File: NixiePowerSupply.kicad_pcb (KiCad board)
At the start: 2 copper layers, 41.5 x 41.5 mm, 20 parts, among them J1 Conn_01x02, J2 Conn_01x02, Q1 IRF740, Q2 2N3905, U1 MC34063AP

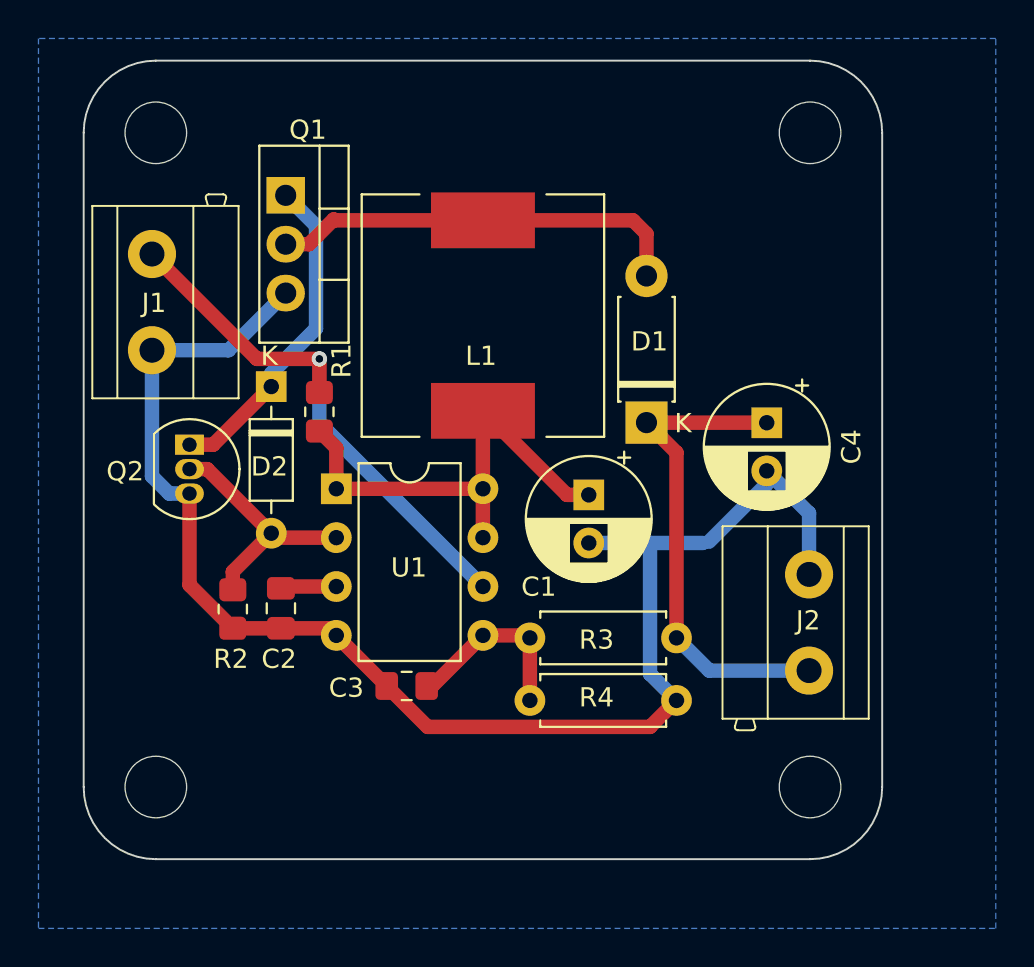
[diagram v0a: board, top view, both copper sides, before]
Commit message: mark input, output
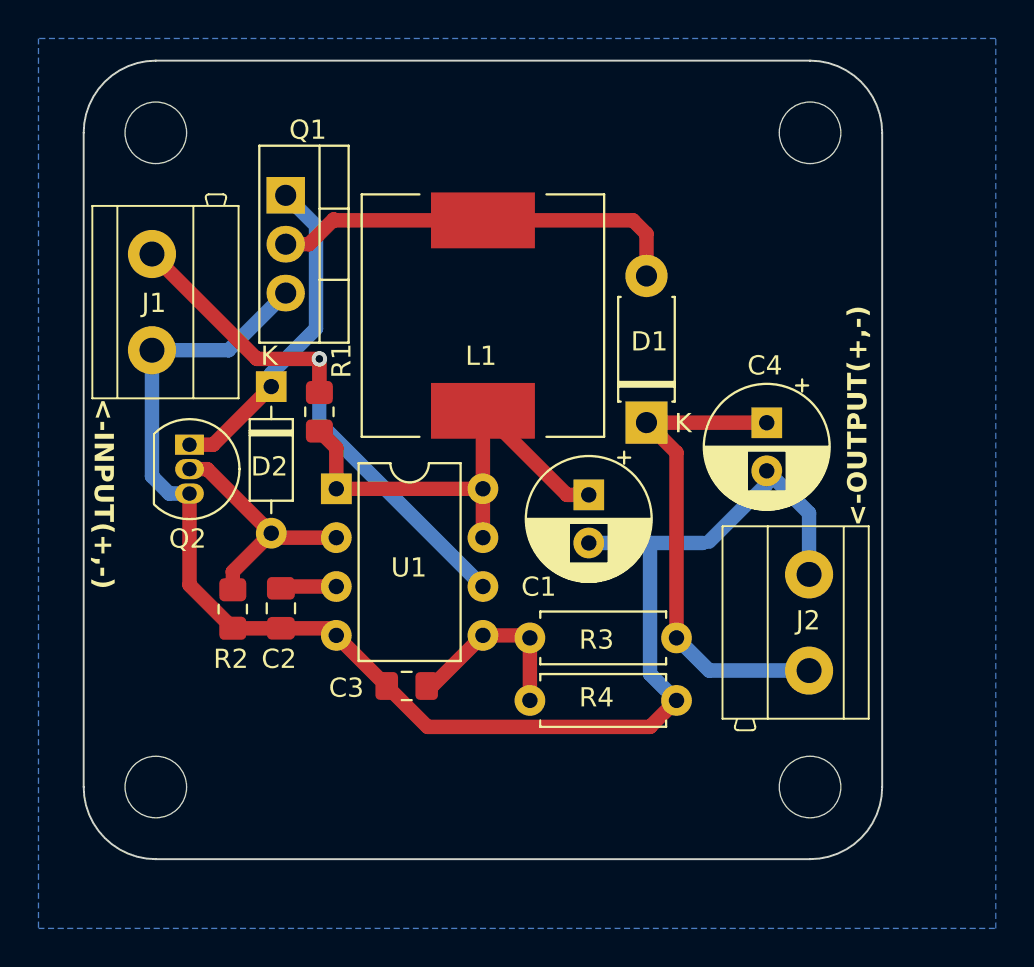
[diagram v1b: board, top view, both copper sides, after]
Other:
- board text added: "<-INPUT(+,-)"
- board text added: "<-OUTPUT(+,-)"
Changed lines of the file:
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@@
     (fp_line (start 1 0.625) (end -1 0.625)
       (stroke (width 0.1) (type solid)) (layer "F.Fab"))
-    (pad "1" smd roundrect (at -1.0375 0 270) (size 1.175 1.45) (layers "F.Cu" "F.Paste" "F.Mask") (roundrect_rratio 0.212766)
+    (pad "1" smd roundrect (at -1.0375 0 270) (size 1.175 1.45) (layers "F.Cu" "F.Paste" "F.Mask") (roundrect_rratio 0.2127659574)
       (net 3 "Net-(U1-TC)") (pintype "passive"))
-    (pad "2" smd roundrect (at 1.0375 0 270) (size 1.175 1.45) (layers "F.Cu" "F.Paste" "F.Mask") (roundrect_rratio 0.212766)
+    (pad "2" smd roundrect (at 1.0375 0 270) (size 1.175 1.45) (layers "F.Cu" "F.Paste" "F.Mask") (roundrect_rratio 0.2127659574)
       (net 2 "GND") (pintype "passive"))
     (model "${KICAD6_3DMODEL_DIR}/Capacitor_SMD.3dshapes/C_0805_2012Metric.wrl"
@@
     (property "ki_keywords" "cap capacitor")
     (attr through_hole)
-    (fp_text reference "C4" (at 1.25 -4.4 90) (layer "F.SilkS")
+    (fp_text reference "C4" (at -2.969271 0.09835 -180) (layer "F.SilkS")
         (effects (font (size 1 1) (thickness 0.15)))
     )
@@
     (fp_line (start 1 0.625) (end -1 0.625)
       (stroke (width 0.1) (type solid)) (layer "F.Fab"))
-    (pad "1" smd roundrect (at -1 0 270) (size 1.2 1.4) (layers "F.Cu" "F.Paste" "F.Mask") (roundrect_rratio 0.208333)
+    (pad "1" smd roundrect (at -1 0 270) (size 1.2 1.4) (layers "F.Cu" "F.Paste" "F.Mask") (roundrect_rratio 0.2083333333)
       (net 9 "Net-(J1-Pin_1)") (pintype "passive"))
-    (pad "2" smd roundrect (at 1 0 270) (size 1.2 1.4) (layers "F.Cu" "F.Paste" "F.Mask") (roundrect_rratio 0.208333)
+    (pad "2" smd roundrect (at 1 0 270) (size 1.2 1.4) (layers "F.Cu" "F.Paste" "F.Mask") (roundrect_rratio 0.2083333333)
       (net 1 "Net-(U1-DC)") (pintype "passive"))
     (model "${KICAD6_3DMODEL_DIR}/Resistor_SMD.3dshapes/R_0805_2012Metric.wrl"
@@
     (fp_line (start 1 0.625) (end -1 0.625)
       (stroke (width 0.1) (type solid)) (layer "F.Fab"))
-    (pad "1" smd roundrect (at -1 0 270) (size 1.2 1.4) (layers "F.Cu" "F.Paste" "F.Mask") (roundrect_rratio 0.208333)
+    (pad "1" smd roundrect (at -1 0 270) (size 1.2 1.4) (layers "F.Cu" "F.Paste" "F.Mask") (roundrect_rratio 0.2083333333)
       (net 8 "Net-(D2-A)") (pintype "passive"))
-    (pad "2" smd roundrect (at 1 0 270) (size 1.2 1.4) (layers "F.Cu" "F.Paste" "F.Mask") (roundrect_rratio 0.208333)
+    (pad "2" smd roundrect (at 1 0 270) (size 1.2 1.4) (layers "F.Cu" "F.Paste" "F.Mask") (roundrect_rratio 0.2083333333)
       (net 2 "GND") (pintype "passive"))
     (model "${KICAD6_3DMODEL_DIR}/Resistor_SMD.3dshapes/R_0805_2012Metric.wrl"
@@
     (property "ki_keywords" "PNP Transistor")
     (attr through_hole)
-    (fp_text reference "Q2" (at 1.38835 3.34835 -180) (layer "F.SilkS")
+    (fp_text reference "Q2" (at 4.88835 0.09835 -180) (layer "F.SilkS")
         (effects (font (size 1 1) (thickness 0.15)))
     )
@@
     (fp_line (start 1 0.625) (end -1 0.625)
       (stroke (width 0.1) (type solid)) (layer "F.Fab"))
-    (pad "1" smd roundrect (at -1.0375 0 180) (size 1.175 1.45) (layers "F.Cu" "F.Paste" "F.Mask") (roundrect_rratio 0.212766)
+    (pad "1" smd roundrect (at -1.0375 0 180) (size 1.175 1.45) (layers "F.Cu" "F.Paste" "F.Mask") (roundrect_rratio 0.2127659574)
       (net 4 "Net-(U1-Vfb)") (pintype "passive"))
-    (pad "2" smd roundrect (at 1.0375 0 180) (size 1.175 1.45) (layers "F.Cu" "F.Paste" "F.Mask") (roundrect_rratio 0.212766)
+    (pad "2" smd roundrect (at 1.0375 0 180) (size 1.175 1.45) (layers "F.Cu" "F.Paste" "F.Mask") (roundrect_rratio 0.2127659574)
       (net 2 "GND") (pintype "passive"))
     (model "${KICAD6_3DMODEL_DIR}/Capacitor_SMD.3dshapes/C_0805_2012Metric.wrl"
@@
   (gr_arc (start 131.09835 150.40165) (mid 130 153.0533) (end 127.34835 154.15165)
     (stroke (width 0.1) (type default)) (layer "Edge.Cuts"))
+  (gr_text "<-INPUT(+,-)" (at 90.04835 130.20165 270) (layer "F.SilkS")
+    (effects (font (size 1 1) (thickness 0.2) bold) (justify left bottom))
+  )
+  (gr_text "<-OUTPUT(+,-)" (at 130.39835 136.85165 90) (layer "F.SilkS")
+    (effects (font (size 1 1) (thickness 0.2) bold) (justify left bottom))
+  )
   (segment (start 114.71597 135.21927) (end 110.34835 130.85165) (width 0.75) (layer "F.Cu") (net 1))
   (segment (start 102.72835 132.78165) (end 101.84835 131.90165) (width 0.75) (layer "F.Cu") (net 1))

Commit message: add logos
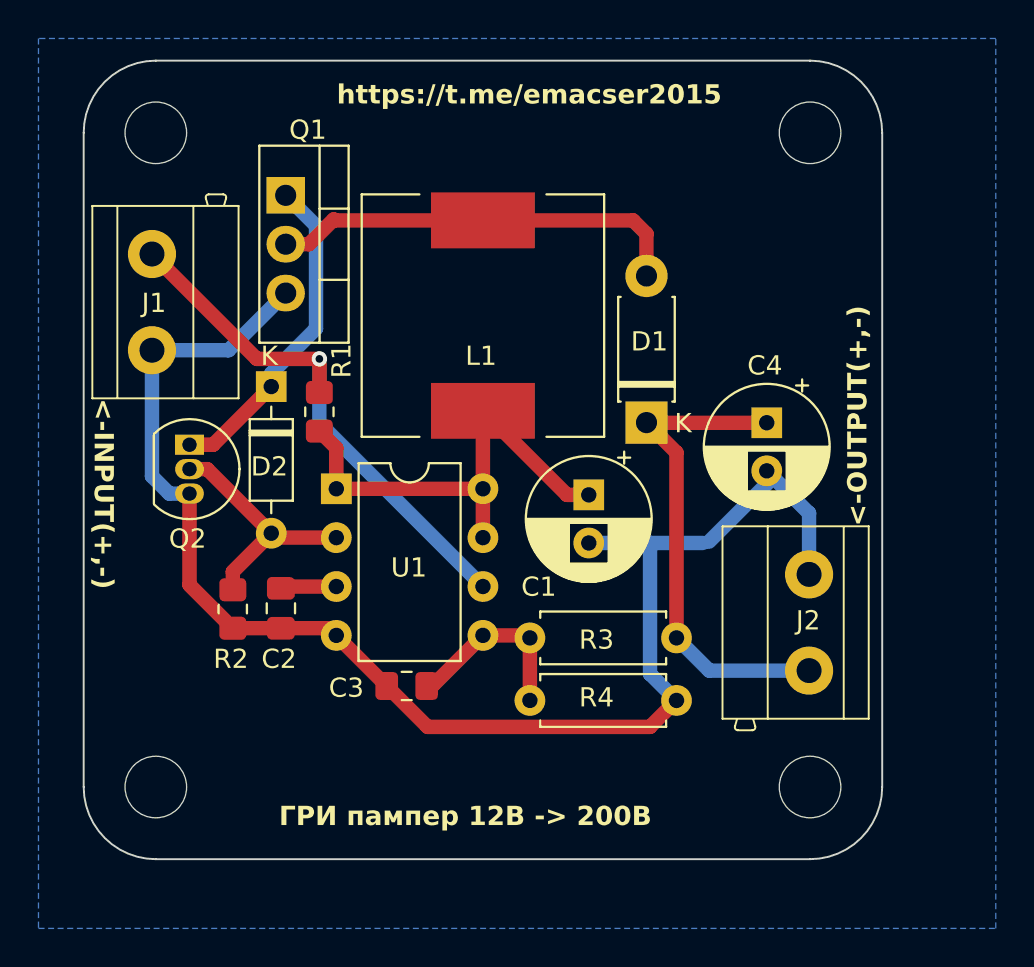
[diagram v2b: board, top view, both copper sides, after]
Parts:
- added G***: LOGO, Library:logo, B.Cu at (102.0, 150.8)
- added REF**: KiCad-Logo2_6mm_SilkScreen, Symbol:KiCad-Logo2_6mm_SilkScreen, B.Cu at (111.2, 116.0)
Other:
- board text added: "https://t.me/emacser2015"
- board text added: "ГРИ пампер 12В -> 200В"

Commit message: add ibom
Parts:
- C1: value C_Polarized -> 220uF 16V LESR Polar 6.3x2.5
- C2: value C -> 2200pF, 0805
- C3: value C -> 0.01uF, 0805
- C4: value C_Polarized -> 2.2uF 250V Polar 6.3x2.5
- D1: value D -> UF4004 UF4007, DO-41
- D2: value D -> 1N4148 1N914, DO-35
- J1, J2: value Conn_01x02 -> DG301-5.0-2P
- L1: value L -> 220uH, 12x12
- Q1: value IRF740 -> IRF740, TO-220
- Q2: value 2N3905 -> MPSA55, TO-92
- R1: value R -> 0.33, 0805
- R2: value R -> 1K, 0805
- R3: value R -> 475K, 1%
- R4: value R -> 3K32, 1%
- U1: value MC34063AP -> MC34063
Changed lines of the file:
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@@
         (effects (font (size 1 1) (thickness 0.15)))
     )
-    (fp_text value "Conn_01x02" (at 0.05 -5.8 90) (layer "F.Fab")
+    (fp_text value "DG301-5.0-2P" (at 0.05 -5.8 90) (layer "F.Fab")
         (effects (font (size 1 1) (thickness 0.15)))
     )
@@
         (effects (font (size 1 1) (thickness 0.15)))
     )
-    (fp_text value "C" (at 0 1.68 90) (layer "F.Fab")
+    (fp_text value "2200pF, 0805" (at 0 1.68 90) (layer "F.Fab")
         (effects (font (size 1 1) (thickness 0.15)))
     )
@@
     (descr "CP, Radial series, Radial, pin pitch=2.50mm, , diameter=6.3mm, Electrolytic Capacitor")
     (tags "CP Radial series Radial pin pitch 2.50mm  diameter 6.3mm Electrolytic Capacitor")
+    (property "Link" "https://www.chipdip.ru/product0/9000565820")
     (property "Sheetfile" "NixiePowerSupply.kicad_sch")
     (property "Sheetname" "")
@@
         (effects (font (size 1 1) (thickness 0.15)))
     )
-    (fp_text value "C_Polarized" (at 1.25 4.4 90) (layer "F.Fab")
+    (fp_text value "2.2uF 250V Polar 6.3x2.5" (at 1.25 4.4 90) (layer "F.Fab")
         (effects (font (size 1 1) (thickness 0.15)))
     )
@@
         (effects (font (size 1 1) (thickness 0.15)))
     )
-    (fp_text value "R" (at 3.81 2.37) (layer "F.Fab")
+    (fp_text value "3K32, 1%" (at 3.81 2.37) (layer "F.Fab")
         (effects (font (size 1 1) (thickness 0.15)))
     )
@@
         (effects (font (size 1 1) (thickness 0.15)))
     )
-    (fp_text value "D" (at 3.81 2.47 90) (layer "F.Fab")
+    (fp_text value "UF4004 UF4007, DO-41" (at 3.81 2.47 90) (layer "F.Fab")
         (effects (font (size 1 1) (thickness 0.15)))
     )
@@
         (effects (font (size 1 1) (thickness 0.15)))
     )
-    (fp_text value "D" (at 3.81 2.12 90) (layer "F.Fab")
+    (fp_text value "1N4148 1N914, DO-35" (at 3.81 2.12 90) (layer "F.Fab")
         (effects (font (size 1 1) (thickness 0.15)))
     )
@@
         (effects (font (size 1 1) (thickness 0.15)))
     )
-    (fp_text value "R" (at 0 1.65 90) (layer "F.Fab")
+    (fp_text value "0.33, 0805" (at 0 1.65 90) (layer "F.Fab")
         (effects (font (size 1 1) (thickness 0.15)))
     )
@@
         (effects (font (size 1 1) (thickness 0.15)))
     )
-    (fp_text value "R" (at 0 1.65 90) (layer "F.Fab")
+    (fp_text value "1K, 0805" (at 0 1.65 90) (layer "F.Fab")
         (effects (font (size 1 1) (thickness 0.15)))
     )
@@
         (effects (font (size 1 1) (thickness 0.15)))
     )
-    (fp_text value "L" (at 0 7.6 90) (layer "F.Fab")
+    (fp_text value "220uH, 12x12" (at 0 7.6 90) (layer "F.Fab")
         (effects (font (size 1 1) (thickness 0.15)))
     )
@@
         (effects (font (size 1 1) (thickness 0.15)))
     )
-    (fp_text value "IRF740" (at 2.54 2.5 90) (layer "F.Fab")
+    (fp_text value "IRF740, TO-220" (at 2.54 2.5 90) (layer "F.Fab")
         (effects (font (size 1 1) (thickness 0.15)))
     )
@@
     (descr "CP, Radial series, Radial, pin pitch=2.50mm, , diameter=6.3mm, Electrolytic Capacitor")
     (tags "CP Radial series Radial pin pitch 2.50mm  diameter 6.3mm Electrolytic Capacitor")
+    (property "Link" "https://www.chipdip.ru/product0/9000565757")
     (property "Sheetfile" "NixiePowerSupply.kicad_sch")
     (property "Sheetname" "")
@@
         (effects (font (size 1 1) (thickness 0.15)))
     )
-    (fp_text value "C_Polarized" (at 1.25 4.4 90) (layer "F.Fab")
+    (fp_text value "220uF 16V LESR Polar 6.3x2.5" (at 1.25 4.4 90) (layer "F.Fab")
         (effects (font (size 1 1) (thickness 0.15)))
     )
@@
         (effects (font (size 1 1) (thickness 0.15)))
     )
-    (fp_text value "MC34063AP" (at 3.81 9.95) (layer "F.Fab")
+    (fp_text value "MC34063" (at 3.81 9.95) (layer "F.Fab")
         (effects (font (size 1 1) (thickness 0.15)))
     )
@@
         (effects (font (size 1 1) (thickness 0.15)))
     )
-    (fp_text value "Conn_01x02" (at 0.05 -5.8 90) (layer "F.Fab")
+    (fp_text value "DG301-5.0-2P" (at 0.05 -5.8 90) (layer "F.Fab")
         (effects (font (size 1 1) (thickness 0.15)))
     )
@@
         (effects (font (size 1 1) (thickness 0.15)))
     )
-    (fp_text value "R" (at 3.81 2.37) (layer "F.Fab")
+    (fp_text value "475K, 1%" (at 3.81 2.37) (layer "F.Fab")
         (effects (font (size 1 1) (thickness 0.15)))
     )
@@
         (effects (font (size 1 1) (thickness 0.15)))
     )
-    (fp_text value "2N3905" (at 1.27 2.79 90) (layer "F.Fab")
+    (fp_text value "MPSA55, TO-92" (at 1.27 2.79 90) (layer "F.Fab")
         (effects (font (size 1 1) (thickness 0.15)))
     )
@@
         (effects (font (size 1 1) (thickness 0.15)))
     )
-    (fp_text value "C" (at 0 1.68) (layer "F.Fab")
-        (effects (font (size 1 1) (thickness 0.15)))
-    )
+    (fp_text value "0.01uF, 0805" (at 0 1.68) (layer "F.Fab")
+        (effects (font (size 1 1) (thickness 0.15)))
+    )

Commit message: fix R3, R4
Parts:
- R3: value 475K, 1% -> 470K, 1%
- R4: value 3K32, 1% -> 3K, 1%
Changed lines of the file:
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@@
         (effects (font (size 1 1) (thickness 0.15)))
     )
-    (fp_text value "3K32, 1%" (at 3.81 2.37) (layer "F.Fab")
+    (fp_text value "3K, 1%" (at 3.81 2.37) (layer "F.Fab")
         (effects (font (size 1 1) (thickness 0.15)))
     )
@@
         (effects (font (size 1 1) (thickness 0.15)))
     )
-    (fp_text value "475K, 1%" (at 3.81 2.37) (layer "F.Fab")
-        (effects (font (size 1 1) (thickness 0.15)))
-    )
+    (fp_text value "470K, 1%" (at 3.81 2.37) (layer "F.Fab")
+        (effects (font (size 1 1) (thickness 0.15)))
+    )

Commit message: fix links in bom
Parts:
- Q2: value MPSA55, TO-92 -> MPSA56, TO-92
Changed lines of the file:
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@@
     (descr "Capacitor SMD 0805 (2012 Metric), square (rectangular) end terminal, IPC_7351 nominal with elongated pad for handsoldering. (Body size source: IPC-SM-782 page 76, https://www.pcb-3d.com/wordpress/wp-content/uploads/ipc-sm-782a_amendment_1_and_2.pdf, https://docs.google.com/spreadsheets/d/1BsfQQcO9C6DZCsRaXUlFlo91Tg2WpOkGARC1WS5S8t0/edit?usp=sharing), generated with kicad-footprint-generator")
     (tags "capacitor handsolder")
+    (property "Link" "https://www.chipdip.ru/product/grm2165c1h222j")
     (property "Sheetfile" "NixiePowerSupply.kicad_sch")
     (property "Sheetname" "")
@@
     (descr "Resistor, Axial_DIN0207 series, Axial, Horizontal, pin pitch=7.62mm, 0.25W = 1/4W, length*diameter=6.3*2.5mm^2, http://cdn-reichelt.de/documents/datenblatt/B400/1_4W%23YAG.pdf")
     (tags "Resistor Axial_DIN0207 series Axial Horizontal pin pitch 7.62mm 0.25W = 1/4W length 6.3mm diameter 2.5mm")
+    (property "Link" "https://aliexpress.ru/item/32847096736.html?spm=a2g2w.orderdetail.0.0.961e4aa6zXOBsP&sku_id=65227930969")
     (property "Sheetfile" "NixiePowerSupply.kicad_sch")
     (property "Sheetname" "")
@@
     (descr "Diode, DO-41_SOD81 series, Axial, Horizontal, pin pitch=7.62mm, , length*diameter=5.2*2.7mm^2, , http://www.diodes.com/_files/packages/DO-41%20(Plastic).pdf")
     (tags "Diode DO-41_SOD81 series Axial Horizontal pin pitch 7.62mm  length 5.2mm diameter 2.7mm")
+    (property "Link" "https://aliexpress.ru/item/4000798077881.html?spm=a2g2w.orderdetail.0.0.635f4aa6UDS5z0&sku_id=10000008048731253")
     (property "Sheetfile" "NixiePowerSupply.kicad_sch")
     (property "Sheetname" "")
@@
     (descr "Resistor SMD 0805 (2012 Metric), square (rectangular) end terminal, IPC_7351 nominal with elongated pad for handsoldering. (Body size source: IPC-SM-782 page 72, https://www.pcb-3d.com/wordpress/wp-content/uploads/ipc-sm-782a_amendment_1_and_2.pdf), generated with kicad-footprint-generator")
     (tags "resistor handsolder")
+    (property "Link" "https://aliexpress.ru/item/1005001794062302.html?spm=a2g2w.orderdetail.0.0.3b194aa6BKKUxl&sku_id=12000017594821115")
     (property "Sheetfile" "NixiePowerSupply.kicad_sch")
     (property "Sheetname" "")
@@
     (descr "Choke, SMD, 12x12mm 8mm height")
     (tags "Choke SMD")
+    (property "Link" "https://aliexpress.ru/item/1005001699203887.html?spm=a2g2w.orderdetail.0.0.1cbb4aa6UPdjMI&sku_id=12000017203437476")
     (property "Sheetfile" "NixiePowerSupply.kicad_sch")
     (property "Sheetname" "")
@@
     (descr "TO-220-3, Vertical, RM 2.54mm, see https://www.vishay.com/docs/66542/to-220-1.pdf")
     (tags "TO-220-3 Vertical RM 2.54mm")
+    (property "Link" "https://www.platan.ru/cgi-bin/qwery.pl/id=318826868")
     (property "Sheetfile" "NixiePowerSupply.kicad_sch")
     (property "Sheetname" "")
@@
     (descr "Resistor, Axial_DIN0207 series, Axial, Horizontal, pin pitch=7.62mm, 0.25W = 1/4W, length*diameter=6.3*2.5mm^2, http://cdn-reichelt.de/documents/datenblatt/B400/1_4W%23YAG.pdf")
     (tags "Resistor Axial_DIN0207 series Axial Horizontal pin pitch 7.62mm 0.25W = 1/4W length 6.3mm diameter 2.5mm")
+    (property "Link" "https://aliexpress.ru/item/32847096736.html?spm=a2g2w.orderdetail.0.0.961e4aa6m8WYZn&sku_id=12000030032474500")
     (property "Sheetfile" "NixiePowerSupply.kicad_sch")
     (property "Sheetname" "")
@@
     (descr "TO-92 leads in-line, narrow, oval pads, drill 0.75mm (see NXP sot054_po.pdf)")
     (tags "to-92 sc-43 sc-43a sot54 PA33 transistor")
+    (property "Link" "https://www.chipdip.ru/product/mpsa56-diotec")
     (property "Sheetfile" "NixiePowerSupply.kicad_sch")
     (property "Sheetname" "")
@@
         (effects (font (size 1 1) (thickness 0.15)))
     )
-    (fp_text value "MPSA55, TO-92" (at 1.27 2.79 90) (layer "F.Fab")
+    (fp_text value "MPSA56, TO-92" (at 1.27 2.79 90) (layer "F.Fab")
         (effects (font (size 1 1) (thickness 0.15)))
     )
@@
     (descr "Capacitor SMD 0805 (2012 Metric), square (rectangular) end terminal, IPC_7351 nominal with elongated pad for handsoldering. (Body size source: IPC-SM-782 page 76, https://www.pcb-3d.com/wordpress/wp-content/uploads/ipc-sm-782a_amendment_1_and_2.pdf, https://docs.google.com/spreadsheets/d/1BsfQQcO9C6DZCsRaXUlFlo91Tg2WpOkGARC1WS5S8t0/edit?usp=sharing), generated with kicad-footprint-generator")
     (tags "capacitor handsolder")
+    (property "Link" "https://www.chipdip.ru/product/grm2195c1h103j")
     (property "Sheetfile" "NixiePowerSupply.kicad_sch")
     (property "Sheetname" "")
